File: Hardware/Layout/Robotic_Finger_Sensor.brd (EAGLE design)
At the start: 14 x 15.2 mm, 9 parts, among them U1 VCNL4040

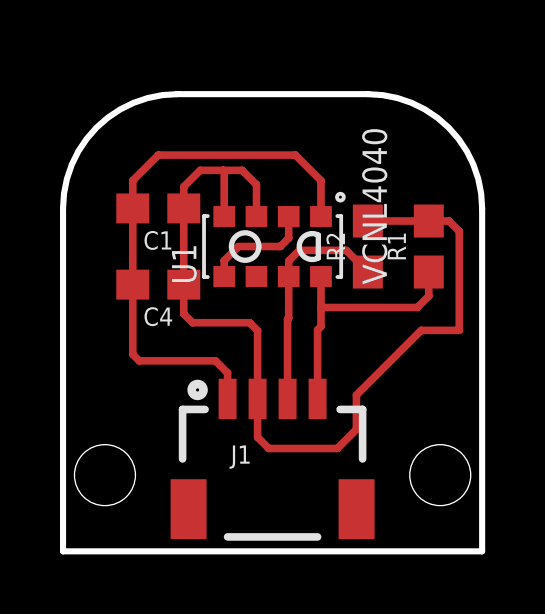
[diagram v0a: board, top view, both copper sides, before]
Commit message: Adding PDF schematic
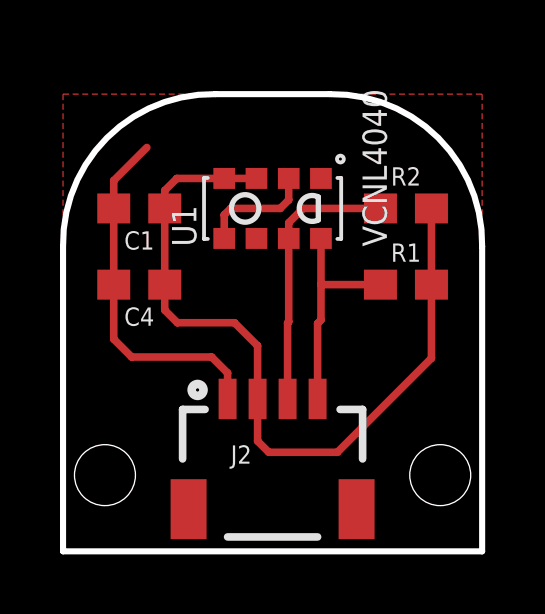
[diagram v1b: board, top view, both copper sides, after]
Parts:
- removed J1: (no value), SparkFun-Connectors:1X04_1MM_RA
- added J2: (no value), SparkX:1X04_1MM_RA
- added U$3, U$4: STAND-OFF, SparkX:STAND-OFF-#2
- U$1: value STAND-OFF -> OSHW-LOGOS; device SparkX:STAND-OFF-#2 -> SparkFun:OSHW-LOGO-S
- U$2: value STAND-OFF -> SPARKX-LOGO3; device SparkX:STAND-OFF-#2 -> SparkX:SPARKX-SMALL
- moved FRAME2 11.7 mm to (-21.6, -20.3)
- moved U$1 10.5 mm to (6.99, 11.4), flipped to the bottom
- moved U$2 5.73 mm to (6.99, 1.27), flipped to the bottom
- moved R2 1.80 mm to (11.4, 11.4), turned to 0 degrees
- moved R1 1.48 mm to (11.4, 8.89), turned to 0 degrees
- moved U1 1.27 mm to (6.99, 11.4)
- moved C1 0.63 mm to (2.54, 11.4)
- moved C4 0.63 mm to (2.54, 8.89)
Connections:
- net 3.3V: now also J2.2; no longer J1.2
- net GND: now also J2.1; no longer J1.1
- net SCL: now also J2.4; no longer J1.4
- net SDA: now also J2.3; no longer J1.3
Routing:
- net GND: track 18.2 -> 12.0 mm
- net 3.3V: track 31.6 -> 26.2 mm
- net SDA: track 7.70 -> 9.14 mm
- net SCL: track 8.68 -> 7.38 mm
- added copper zone on layer 1, net GND
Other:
- outline, holes or cut-outs redrawn
- board text added: "N. Seidle"
- board text added: "Robotic Finger Sensor"
